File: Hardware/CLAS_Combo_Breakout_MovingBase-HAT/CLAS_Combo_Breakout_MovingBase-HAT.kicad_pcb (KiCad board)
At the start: 4 copper layers, 38.5 x 60 mm, 60 parts, among them J1 MMCX, J2 SMA, J3 SWD, J4 ZED, J5 BATT, J6 NEO, J7 USB_C_Receptacle_USB2.0, Q1 AO3415A, SW1 SW_Push, SW2 SW_SPDT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

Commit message: ちょっと配線した
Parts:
- removed C3: 0.1u, Capacitor_SMD:C_0603_1608Metric
- removed H4: MH, MountingHole:MountingHole_2.2mm_M2_Pad_Via
- J6: footprint Connector_PinHeader_2.54mm:PinHeader_1x09_P2.54mm_Vertical -> Connector_PinHeader_2.54mm:PinHeader_1x07_P2.54mm_Vertical
- moved R9 36.4 mm to (129.0, 123.6), turned to -90 degrees
- moved D5 33.8 mm to (125.9, 123.6), turned to -90 degrees
- moved D6 33.1 mm to (129.0, 126.6), turned to 90 degrees
- moved R8 31.5 mm to (125.9, 126.6), turned to 90 degrees
- moved D4 31.1 mm to (127.5, 123.6), turned to -90 degrees
- moved R7 28.7 mm to (127.5, 126.6), turned to 90 degrees
- moved D1 14.1 mm to (128.5, 111.9), turned to 180 degrees
- moved R3 6.12 mm to (135.1, 114.9), turned to 0 degrees
- moved SW1 5.68 mm to (140.2, 117.0), turned to -90 degrees
- moved C6 3.97 mm to (135.1, 116.4), turned to 0 degrees
- moved C7 3.25 mm to (140.7, 112.4), turned to 90 degrees
- moved U6 3.09 mm to (139.1, 109.8)
- moved J3 2.65 mm to (138.9, 101.7)
- moved R11 2.41 mm to (139.1, 130.9), turned to -90 degrees
- moved R1 2.27 mm to (140.2, 124.1), turned to 45 degrees
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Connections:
- U3 pad 11: /~{VBAT_EN} -> /GEO
- U3 pad 12: /VBAT -> /~{VBAT_EN}
- U3 pad 13: /GEO -> /VBAT
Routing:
- net /GEO: track 0.00 -> 35.6 mm, vias 0 -> 1
- net /RTK: track 0.00 -> 31.6 mm, vias 0 -> 1
- net /TP: track 0.00 -> 28.0 mm, vias 0 -> 1
- net /EXTINT_ZED: track 0.00 -> 27.2 mm, vias 0 -> 1
- net +3.3V: track 32.3 -> 59.5 mm, vias 0 -> 1
- net /TXD1_ZED: track 0.00 -> 26.8 mm
- net /TX_RDY: track 0.00 -> 26.7 mm, vias 0 -> 1
- net /RXD1_ZED: track 0.00 -> 26.4 mm
- net /~{VBAT_EN}: track 0.00 -> 11.2 mm
- net /DTR: track 10.5 -> 0.00 mm
- net /nRF52_RXD: track 0.00 -> 8.35 mm
- net /VBAT: track 1.49 -> 9.59 mm
- net /ZED_UART_EN: track 0.00 -> 6.82 mm
- net /~{CHG_STAT}: track 5.39 -> 10.3 mm
- net VBUS: track 10.5 -> 13.9 mm, vias 0 -> 1
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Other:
- board text added: "F9PのUARTをコネクタで引き出す I2Cも引き出す"
- board text added: "翼端灯LED用コネクタ"

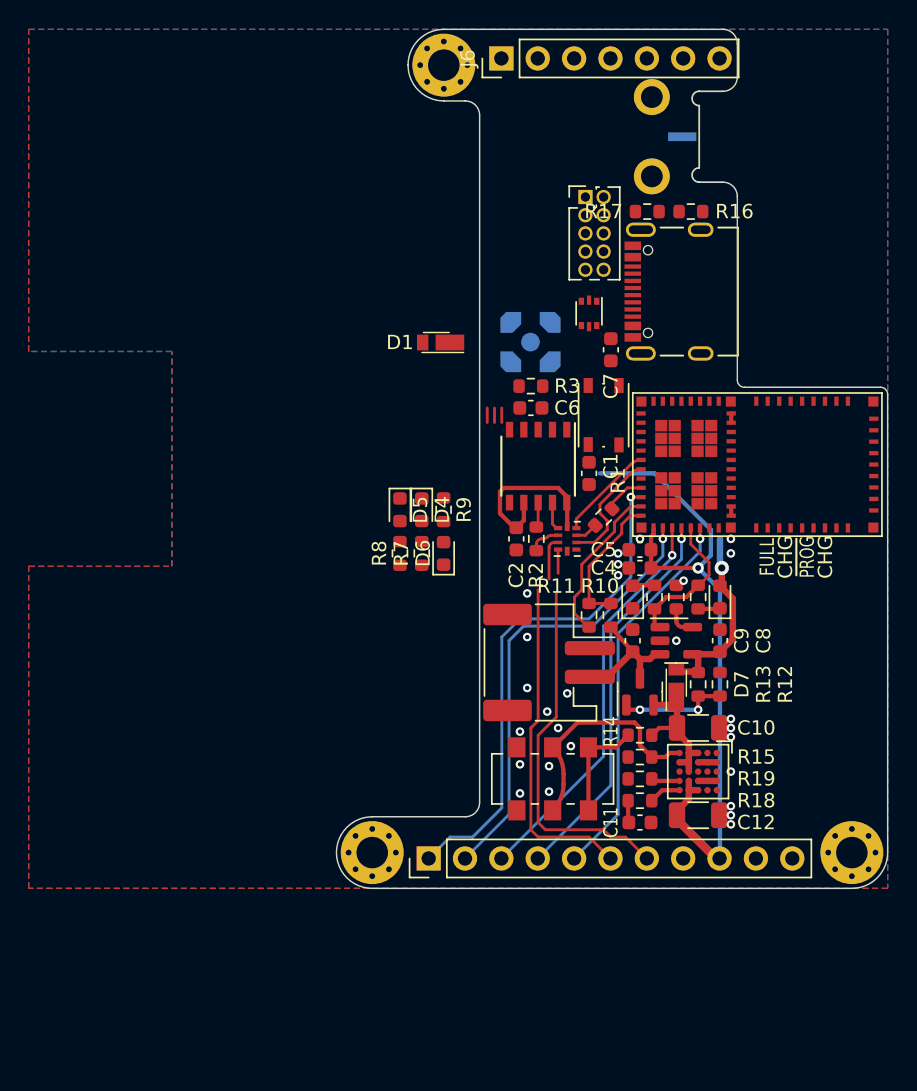
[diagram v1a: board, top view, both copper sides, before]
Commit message: MUXをSP3Tのものに変更しRS485経由での補正データの送受信に対応する回路図を書いた
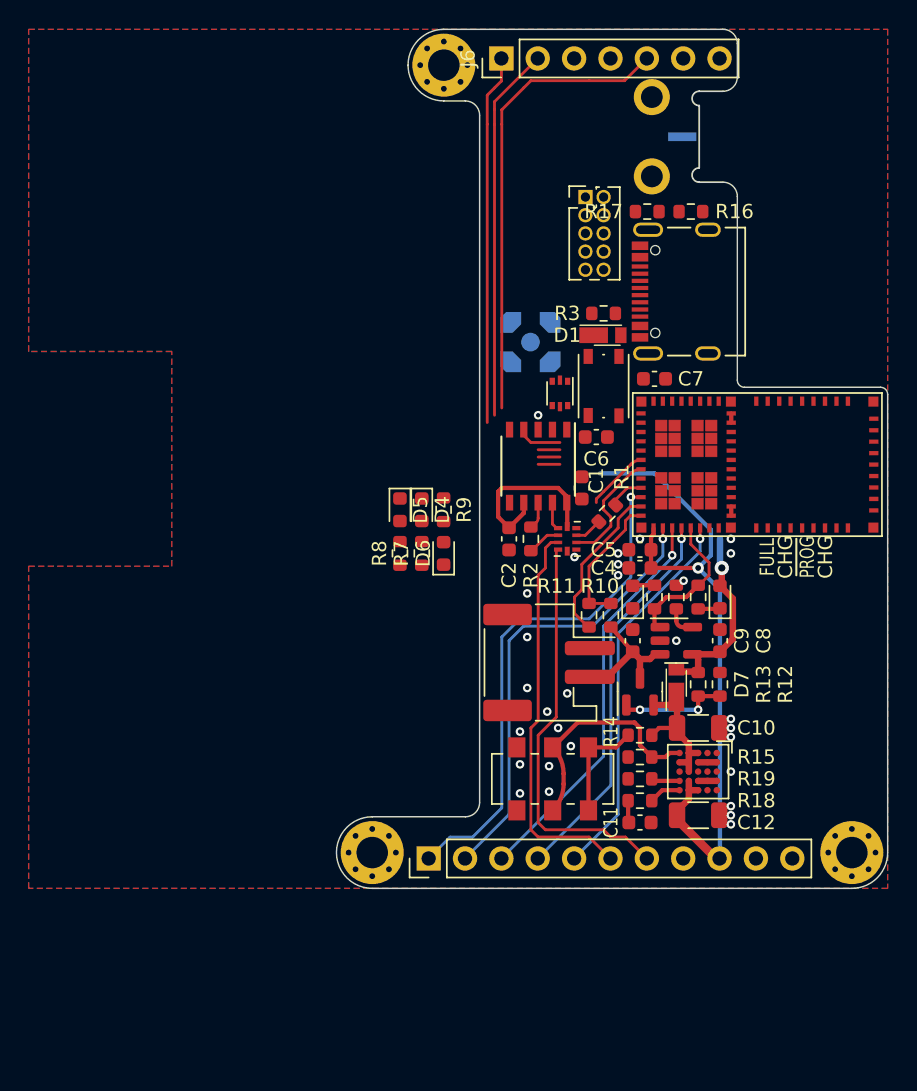
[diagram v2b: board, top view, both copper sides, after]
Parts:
- moved D1 11.9 mm to (140.4, 111.4), turned to 0 degrees
- moved R3 7.18 mm to (140.2, 109.8)
- moved U6 5.95 mm to (137.1, 115.4)
- moved C6 5.00 mm to (139.7, 118.5)
- moved C7 3.66 mm to (143.7, 114.4), turned to 180 degrees
- moved SW1 2.03 mm to (140.2, 114.9)
- moved C1 1.14 mm to (138.6, 122.0)
- moved J7 0.51 mm to (145.2, 108.3)
- moved C2 0.51 mm to (133.6, 125.6)
- moved R2 0.38 mm to (135.1, 125.6)
- moved R1 0.36 mm to (140.4, 123.8)
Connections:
- U3 pad 3: /RESET_ZED_NEO -> /EXTINT_NEO
- U3 pad 4: /EXTANT_DETECT -> /RESET_ZED_NEO
- U3 pad 6: /EXTINT_NEO -> /EXTANT_DETECT
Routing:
- net /EXTINT_NEO: track 0.00 -> 34.0 mm
- net /RESET_ZED_NEO: track 0.00 -> 27.7 mm
- net /EXTANT_DETECT: track 0.00 -> 27.4 mm
- net /DTR: track 0.00 -> 3.13 mm
- net (no net): track 3.05 -> 0.00 mm
- net /ZED_UART_EN: track 6.82 -> 4.46 mm
- net /TXD1_ZED: track 26.8 -> 28.3 mm
- net /RXD1_ZED: track 26.4 -> 27.5 mm
- net GND: vias 27 -> 29
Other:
- board text added: "EXTINTとRESETに抵抗付けて切断できるようにする"
- board text added: "I2Cを引き出す"
- board text removed: "F9PのUARTをコネクタで引き出す I2Cも引き出す"

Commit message: 一部ライブラリを整理
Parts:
- added C13: 0.1u, Capacitor_SMD:C_0603_1608Metric, F.Cu at (139.7, 127.6)
- added C3: 0.1u, Capacitor_SMD:C_0603_1608Metric, F.Cu at (139.7, 123.0)
- added J8: RS485, Connector_JST:JST_PH_S3B-PH-K_1x03_P2.00mm_Horizontal, B.Cu at (139.7, 103.2)
- added R20: 10k, Resistor_SMD:R_0603_1608Metric, F.Cu at (138.4, 123.0)
- added R21: 10k, Resistor_SMD:R_0603_1608Metric, F.Cu at (137.1, 123.0)
- added R22: 10k, Resistor_SMD:R_0603_1608Metric, F.Cu at (133.6, 127.6)
- added R23: 10k, Resistor_SMD:R_0603_1608Metric, F.Cu at (136.6, 127.6)
- added R24: 120, Resistor_SMD:R_0603_1608Metric, F.Cu at (140.7, 129.7)
- added U7: MAX3485, Package_SO:SOIC-8_3.9x4.9mm_P1.27mm, F.Cu at (136.1, 131.2)
- J5: footprint Connector_JST:JST_PH_S2B-PH-SM4-TB_1x02-1MP_P2.00mm_Horizontal -> Connector_JST:JST_PH_S2B-PH-K_1x02_P2.00mm_Horizontal; moved to B.Cu
- U2: value TMUX136 -> TMUX131; footprint Package_DFN_QFN:Texas_R-PUQFN-N10 -> Package_DFN_QFN_extlib:Texas_RMG0012A_1.8x1.8mm_P0.4mm
- moved J5 23.1 mm to (139.7, 111.4)
- moved R9 18.3 mm to (128.0, 141.8)
- moved D6 15.5 mm to (126.4, 141.8), turned to -90 degrees
- moved D4 15.3 mm to (126.4, 138.8)
- moved D5 12.2 mm to (126.4, 135.7)
- moved R7 12.2 mm to (128.0, 138.8), turned to -90 degrees
- moved R8 9.37 mm to (128.0, 135.7), turned to -90 degrees
- moved D1 9.24 mm to (139.1, 120.5)
- moved R3 9.16 mm to (140.7, 119.0)
- moved R16 7.22 mm to (141.7, 108.3), turned to 90 degrees
- moved U6 6.78 mm to (143.7, 113.9), turned to 180 degrees
- moved R11 5.91 mm to (136.6, 136.3), turned to 180 degrees
- moved J3 5.73 mm to (137.6, 107.3), turned to -90 degrees
- moved R10 5.43 mm to (139.7, 136.3), turned to 180 degrees
- moved C1 4.77 mm to (134.3, 124.1), turned to 180 degrees
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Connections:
- J3 pad 6: unconnected-(J3-Pad6) -> /SWO
- U2 pad 1: /CH340K_RXD -> /RoverMode
- U2 pad 10: +3.3V -> /nRF52_RXD
- U2 pad 2: /CH340K_TXD -> /BaseMode
- U2 pad 3: /RXD1_ZED -> /CH340K_RXD
- U2 pad 4: /TXD1_ZED -> /CH340K_TXD
- U2 pad 5: GND -> /RXD1_ZED
- U2 pad 6: GND -> /RS485_TXD
- U2 pad 7: /nRF52_RXD -> /RS485_RXD
- U2 pad 8: /nRF52_TXD -> /TXD1_ZED
- U2 pad 9: /ZED_UART_EN -> GND
- U3 pad 41: unconnected-(U3-Pad41) -> /SWO
- U3 pad 7: /ZED_UART_EN -> /RoverMode
- U3 pad 9: unconnected-(U3-Pad9) -> /BaseMode
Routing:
- net /EXTANT_DETECT: track 27.4 -> 5.01 mm
- net /RESET_ZED_NEO: track 27.7 -> 5.85 mm
- net /RXD1_ZED: track 27.5 -> 5.78 mm
- net /EXTINT_NEO: track 34.0 -> 12.6 mm
- net /TXD1_ZED: track 28.3 -> 7.91 mm
- net +3.3V: track 59.6 -> 43.5 mm
- net Net-(R15-Pad1): track 16.2 -> 4.97 mm
- net /~{VBAT_EN}: track 11.2 -> 1.96 mm
- net /VBAT: track 9.59 -> 1.23 mm
- net /nRF52_RXD: track 8.35 -> 0.00 mm
- net Net-(R14-Pad2): track 7.52 -> 0.00 mm
- net +BATT: track 9.61 -> 3.59 mm
- net /ZED_UART_EN: track 4.46 -> 0.00 mm
- net /DTR: track 3.13 -> 0.00 mm
- net /CH340K_TXD: track 2.35 -> 0.00 mm
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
